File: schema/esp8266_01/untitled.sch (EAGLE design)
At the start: 15 parts, among them IC1 LD117AS33TR, X1 22-23-2021

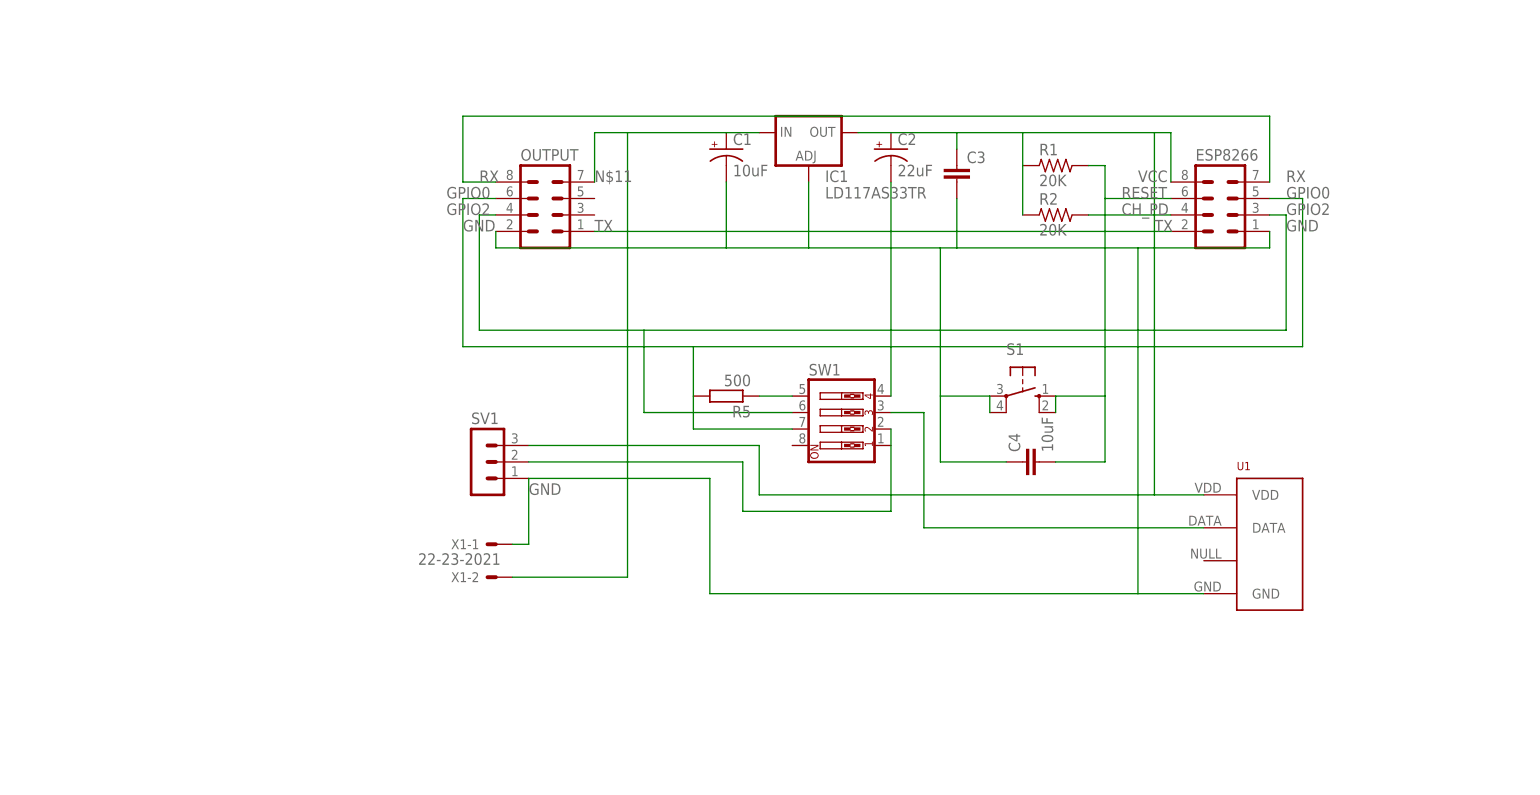
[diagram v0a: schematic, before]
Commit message: Added ch340
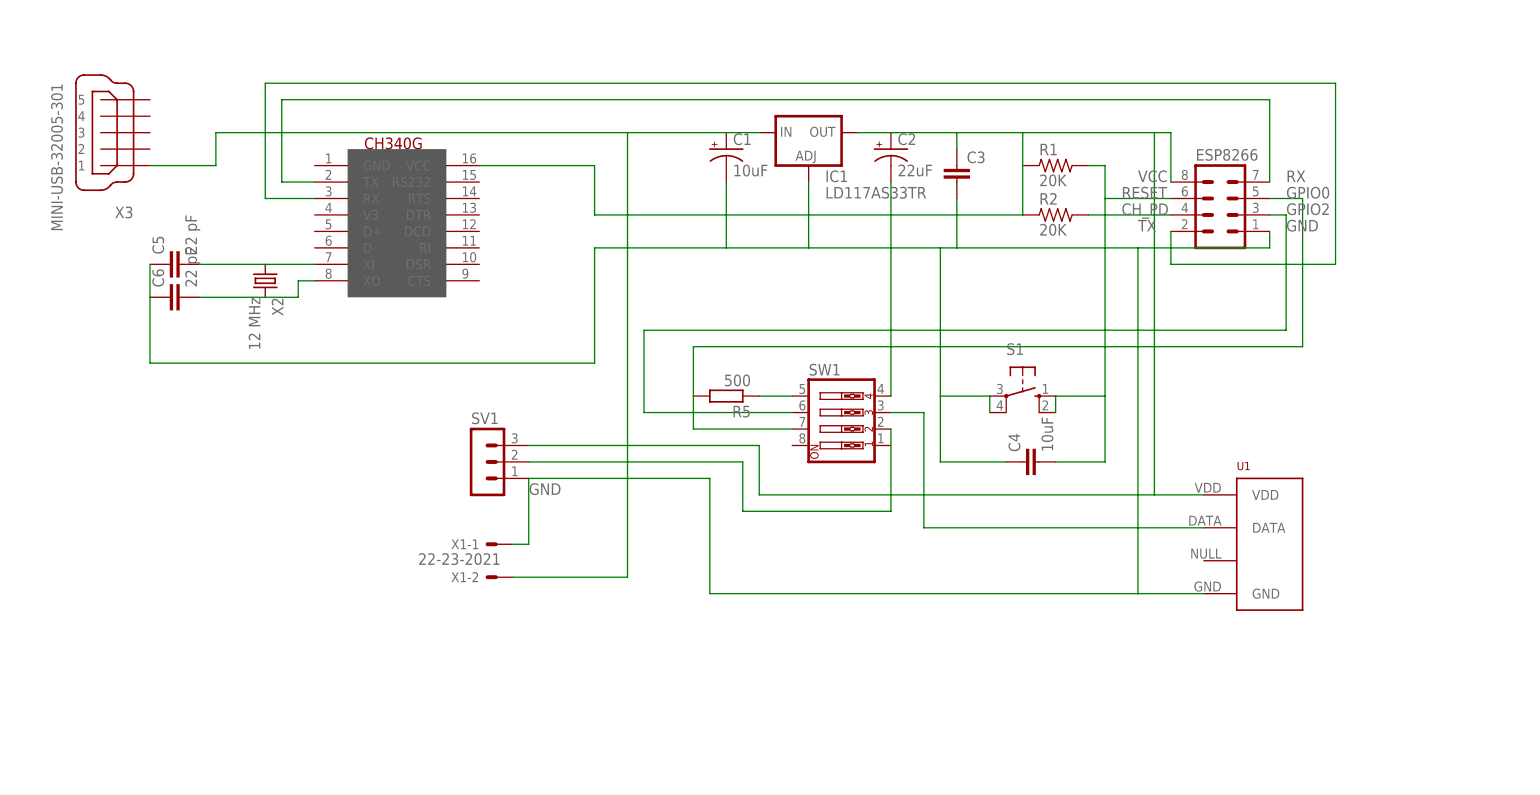
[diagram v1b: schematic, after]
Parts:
- removed OUTPUT: (no value), con-lstb:MA04-2
- added C5, C6: 22 pF, rcl:C-EUC0805
- added U$1: CH340G, usb-serial:CH340G
- added X2: 12 MHz, IQD-Frequency-Products:CRYSTALS-NOGND-HC49
- added X3: MINI-USB-32005-301, con-cypressindustries:MINI-USB-32005-301
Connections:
- new net N$27: C5.2, U$1.XI, X2.1
- new net N$28: C6.2, U$1.XO, X2.2
- net GND: now also C5.1, C6.1; no longer OUTPUT.2
- net GPIO0: no longer OUTPUT.6
- net GPIO2: no longer OUTPUT.4
- net N$11: now also X3.1; no longer OUTPUT.7
- net RX: now also U$1.TX; no longer OUTPUT.8
- net TX: now also U$1.RX; no longer OUTPUT.1
- net VCC: now also U$1.VCC

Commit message: Added normal dht22 lib. Fixed known issues. looks like stable
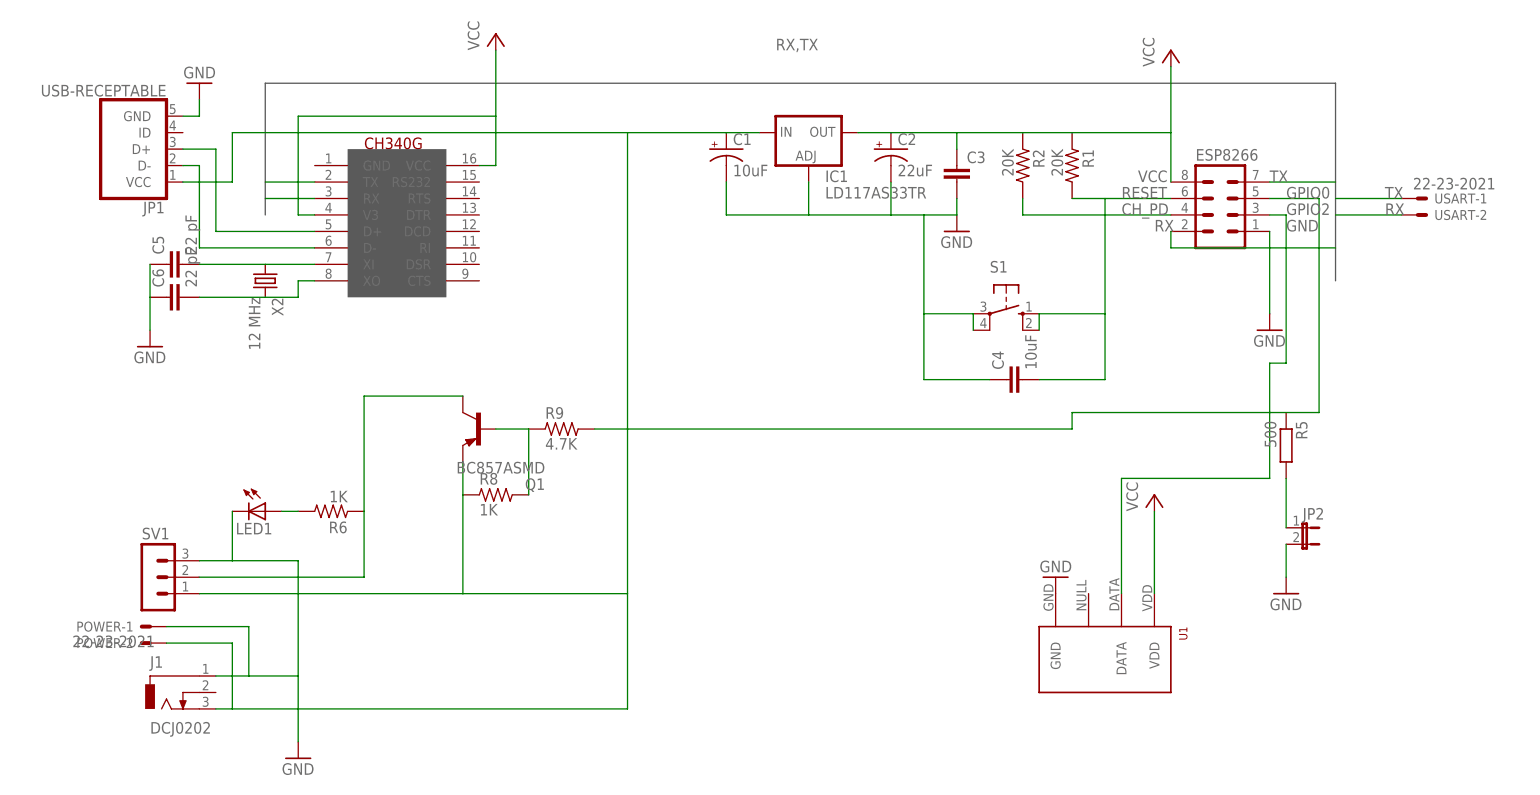
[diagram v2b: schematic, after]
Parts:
- removed SW1: (no value), special:SW_DIP-4
- removed X1: 22-23-2021, con-molex:22-23-2021
- removed X3: MINI-USB-32005-301, con-cypressindustries:MINI-USB-32005-301
- added J1: DCJ0202, con-jack:DCJ0202
- added JP1: USB-RECEPTABLE, daspilker:USB-RECEPTABLE
- added JP2: (no value), jumper:JP1E
- added LED1: (no value), led:LED3MM
- added POWER, USART: 22-23-2021, con-molex:22-23-2021
- added Q1: BC857ASMD, transistor-pnp:BC857ASMD
- added R6, R8: 1K, rc-master:R_0805
- added R9: 4.7K, rc-master:R_0805
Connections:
- removed net N$11: C1.+, IC1.IN, X1-2.S, X3.1
- new net N$29: JP1.D-, U$1.D-
- new net N$31: JP1.D+, U$1.D+
- new net N$32: LED1.A, R6.2
- new net N$37: C1.+, IC1.IN, J1.3, JP1.VCC, POWER-2.S, Q1.E, R8.1, SV1.1
- net GND: now also J1.1, JP1.GND, JP2.2, LED1.C, POWER-1.S, SV1.3; no longer SV1.1, SW1.4, X1-1.S
- net GPIO0: now also R5.1, R9.2; no longer R5.2, SW1.7
- net GPIO2: now also U1.DATA; no longer SW1.6
- net N$1: now also JP2.1, R5.2; no longer R5.1, SW1.5
- net N$3: now also Q1.B, R8.2, R9.1; no longer SW1.3, U1.DATA
- net N$7: now also Q1.C, R6.1; no longer SW1.2
- net RX: now also ESP8266.2, U$1.RX, USART-2.S; no longer ESP8266.7, U$1.TX
- net TX: now also ESP8266.7, U$1.TX, USART-1.S; no longer ESP8266.2, U$1.RX
- net VCC: now also U$1.V3; no longer SV1.3
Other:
- moved on the sheet: C4, R1, R2, R5, S1, SV1, U1

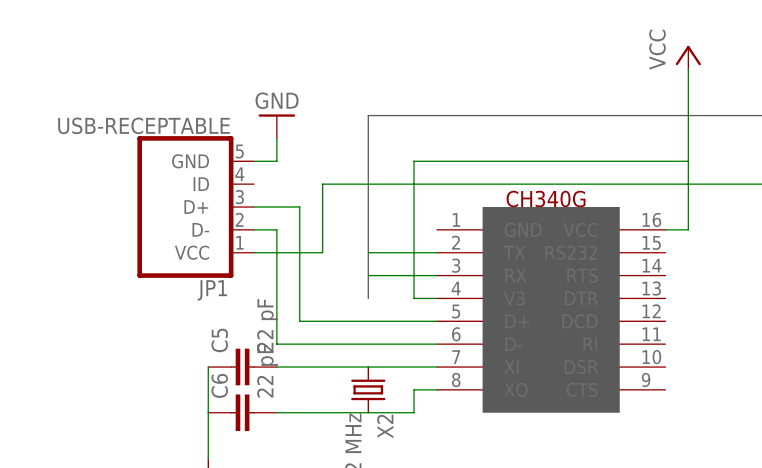
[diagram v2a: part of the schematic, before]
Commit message: Added second variant of esp8266
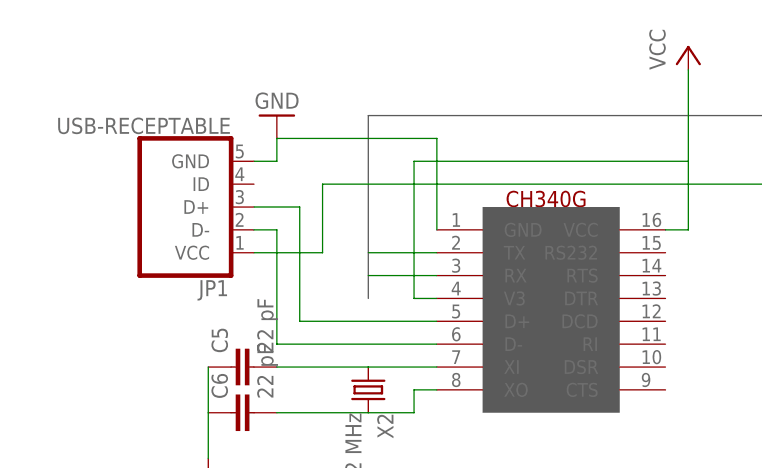
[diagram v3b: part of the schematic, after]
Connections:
- net GND: now also U$1.GND
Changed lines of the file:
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@@
 <wire x1="-55.88" y1="68.58" x2="-53.34" y2="68.58" width="0.1524" layer="91"/>
 <wire x1="-53.34" y1="68.58" x2="-53.34" y2="71.12" width="0.1524" layer="91"/>
+<pinref part="U$1" gate="G$1" pin="GND"/>
+<wire x1="-35.56" y1="60.96" x2="-35.56" y2="71.12" width="0.1524" layer="91"/>
+<wire x1="-35.56" y1="71.12" x2="-53.34" y2="71.12" width="0.1524" layer="91"/>
 </segment>
 <segment>

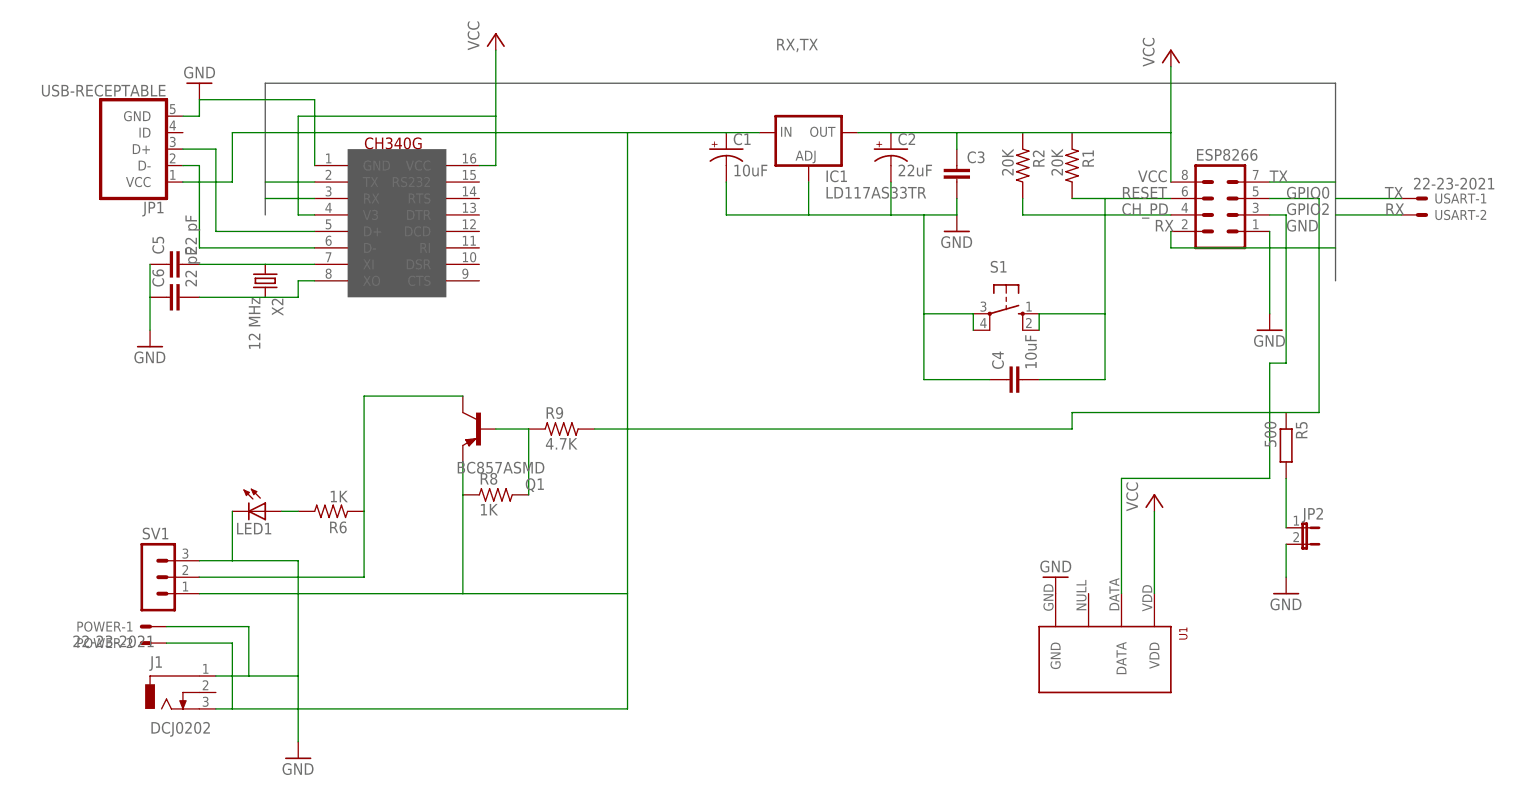
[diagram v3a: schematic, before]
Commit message: Minimised schema var 1
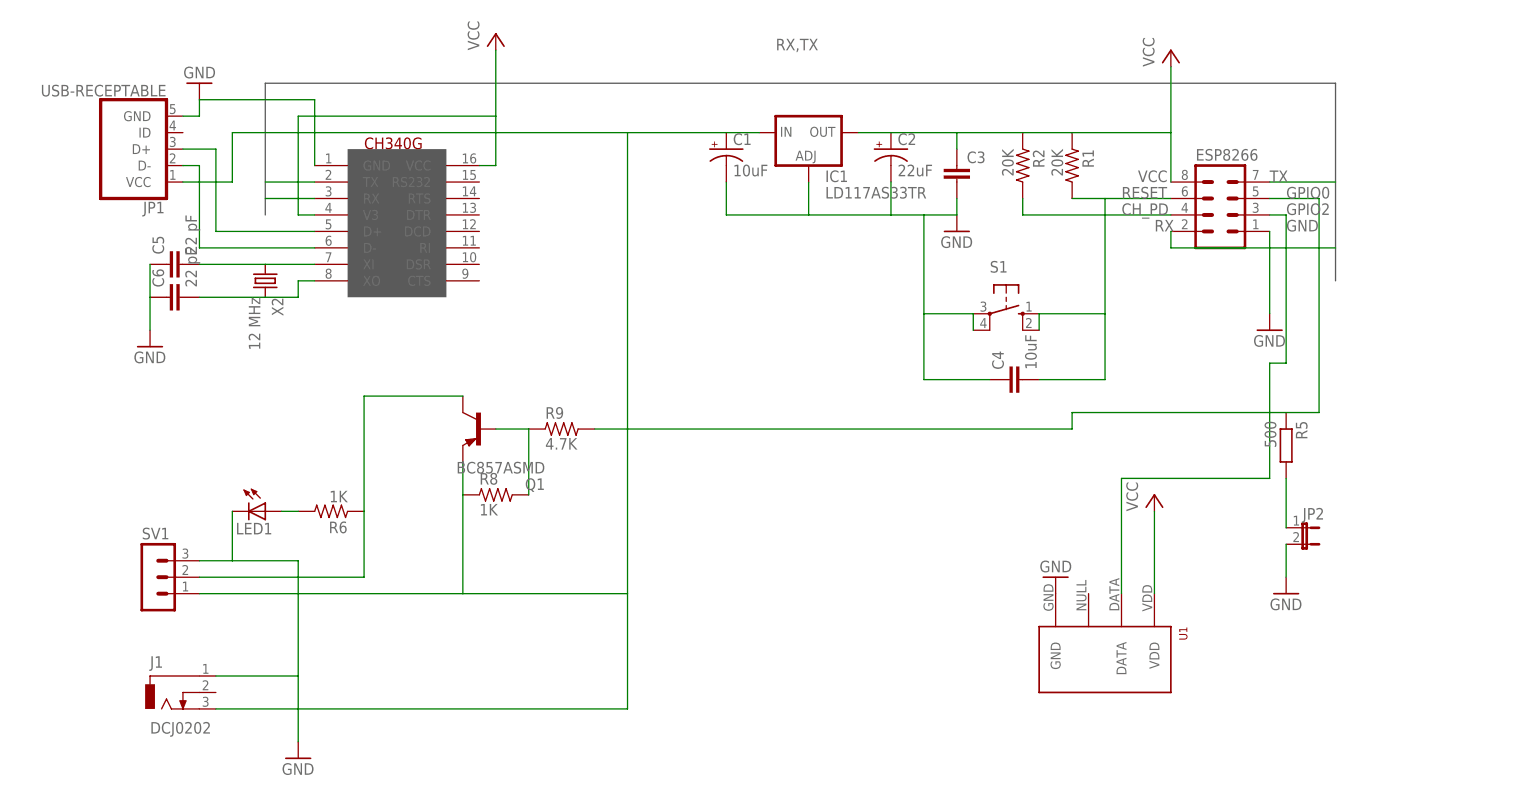
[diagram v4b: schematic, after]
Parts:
- removed POWER, USART: 22-23-2021, con-molex:22-23-2021
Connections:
- net GND: no longer POWER-1.S
- net N$37: no longer POWER-2.S
- net RX: no longer USART-2.S
- net TX: no longer USART-1.S
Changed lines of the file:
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@@
 <part name="JP1" library="daspilker" deviceset="USB-RECEPTABLE" device=""/>
 <part name="GND7" library="supply1" deviceset="GND" device=""/>
-<part name="USART" library="con-molex" deviceset="22-23-2021" device="">
-<attribute name="MPN" value="usart"/>
-</part>
 <part name="J1" library="con-jack" deviceset="DCJ0202" device=""/>
 <part name="LED1" library="led" deviceset="LED" device="3MM"/>
 <part name="R6" library="rc-master" deviceset="R_" device="0805" value="1K"/>
-<part name="POWER" library="con-molex" deviceset="22-23-2021" device="">
-<attribute name="MPN" value="usart"/>
-</part>
 <part name="JP2" library="jumper" deviceset="JP1E" device=""/>
 <part name="Q1" library="transistor-pnp" deviceset="BC857*" device="SMD" technology="A"/>
@@
 <instance part="JP1" gate="G$1" x="-63.5" y="63.5" rot="R180"/>
 <instance part="GND7" gate="1" x="-53.34" y="73.66" rot="R180"/>
-<instance part="USART" gate="-1" x="134.62" y="55.88"/>
-<instance part="USART" gate="-2" x="134.62" y="53.34"/>
 <instance part="J1" gate="G$1" x="-58.42" y="-20.32"/>
 <instance part="LED1" gate="G$1" x="-43.18" y="7.62" rot="R270"/>
 <instance part="R6" gate="G$1" x="-33.02" y="7.62" rot="R180"/>
-<instance part="POWER" gate="-1" x="-60.96" y="-10.16" rot="R180"/>
-<instance part="POWER" gate="-2" x="-60.96" y="-12.7" rot="R180"/>
 <instance part="JP2" gate="A" x="116.84" y="5.08" rot="R270"/>
 <instance part="Q1" gate="G$1" x="-10.16" y="20.32" rot="R180"/>
@@
 <wire x1="-38.1" y1="0" x2="-48.26" y2="0" width="0.1524" layer="91"/>
 <wire x1="-48.26" y1="0" x2="-53.34" y2="0" width="0.1524" layer="91"/>
-<wire x1="-50.8" y1="-17.78" x2="-45.72" y2="-17.78" width="0.1524" layer="91"/>
-<wire x1="-45.72" y1="-17.78" x2="-38.1" y2="-17.78" width="0.1524" layer="91"/>
-<pinref part="POWER" gate="-1" pin="S"/>
-<wire x1="-58.42" y1="-10.16" x2="-45.72" y2="-10.16" width="0.1524" layer="91"/>
-<wire x1="-45.72" y1="-10.16" x2="-45.72" y2="-17.78" width="0.1524" layer="91"/>
+<wire x1="-50.8" y1="-17.78" x2="-38.1" y2="-17.78" width="0.1524" layer="91"/>
 <pinref part="LED1" gate="G$1" pin="C"/>
 <wire x1="-48.26" y1="7.62" x2="-48.26" y2="0" width="0.1524" layer="91"/>
@@
 <label x="111.76" y="58.42" size="1.778" layer="95"/>
 </segment>
-<segment>
-<pinref part="USART" gate="-1" pin="S"/>
-<wire x1="121.92" y1="55.88" x2="132.08" y2="55.88" width="0.1524" layer="91"/>
-<label x="129.54" y="55.88" size="1.778" layer="95"/>
-</segment>
 </net>
 <net name="RX" class="0">
@@
 <wire x1="96.52" y1="48.26" x2="96.52" y2="50.8" width="0.1524" layer="91"/>
 <label x="93.98" y="50.8" size="1.778" layer="95"/>
-</segment>
-<segment>
-<pinref part="USART" gate="-2" pin="S"/>
-<wire x1="121.92" y1="53.34" x2="132.08" y2="53.34" width="0.1524" layer="91"/>
-<label x="129.54" y="53.34" size="1.778" layer="95"/>
 </segment>
 </net>
@@
 <wire x1="-48.26" y1="66.04" x2="12.7" y2="66.04" width="0.1524" layer="91"/>
 <pinref part="J1" gate="G$1" pin="3"/>
-<wire x1="-50.8" y1="-22.86" x2="-48.26" y2="-22.86" width="0.1524" layer="91"/>
-<wire x1="-48.26" y1="-22.86" x2="12.7" y2="-22.86" width="0.1524" layer="91"/>
+<wire x1="-50.8" y1="-22.86" x2="12.7" y2="-22.86" width="0.1524" layer="91"/>
 <wire x1="12.7" y1="-22.86" x2="12.7" y2="-5.08" width="0.1524" layer="91"/>
-<pinref part="POWER" gate="-2" pin="S"/>
-<wire x1="-58.42" y1="-12.7" x2="-48.26" y2="-12.7" width="0.1524" layer="91"/>
-<wire x1="-48.26" y1="-12.7" x2="-48.26" y2="-22.86" width="0.1524" layer="91"/>
 <wire x1="-12.7" y1="10.16" x2="-12.7" y2="-5.08" width="0.1524" layer="91"/>
 </segment>
